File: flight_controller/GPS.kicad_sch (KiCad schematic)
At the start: 25 parts, among them CN2 A1251WV-S-6P, CN3 A1251WV-S-4P, CN5 A1251WV-S-3P, J16 A1257WV-S-6P-LCP, J17 HCZZ0494-2, Q2 AO3400A

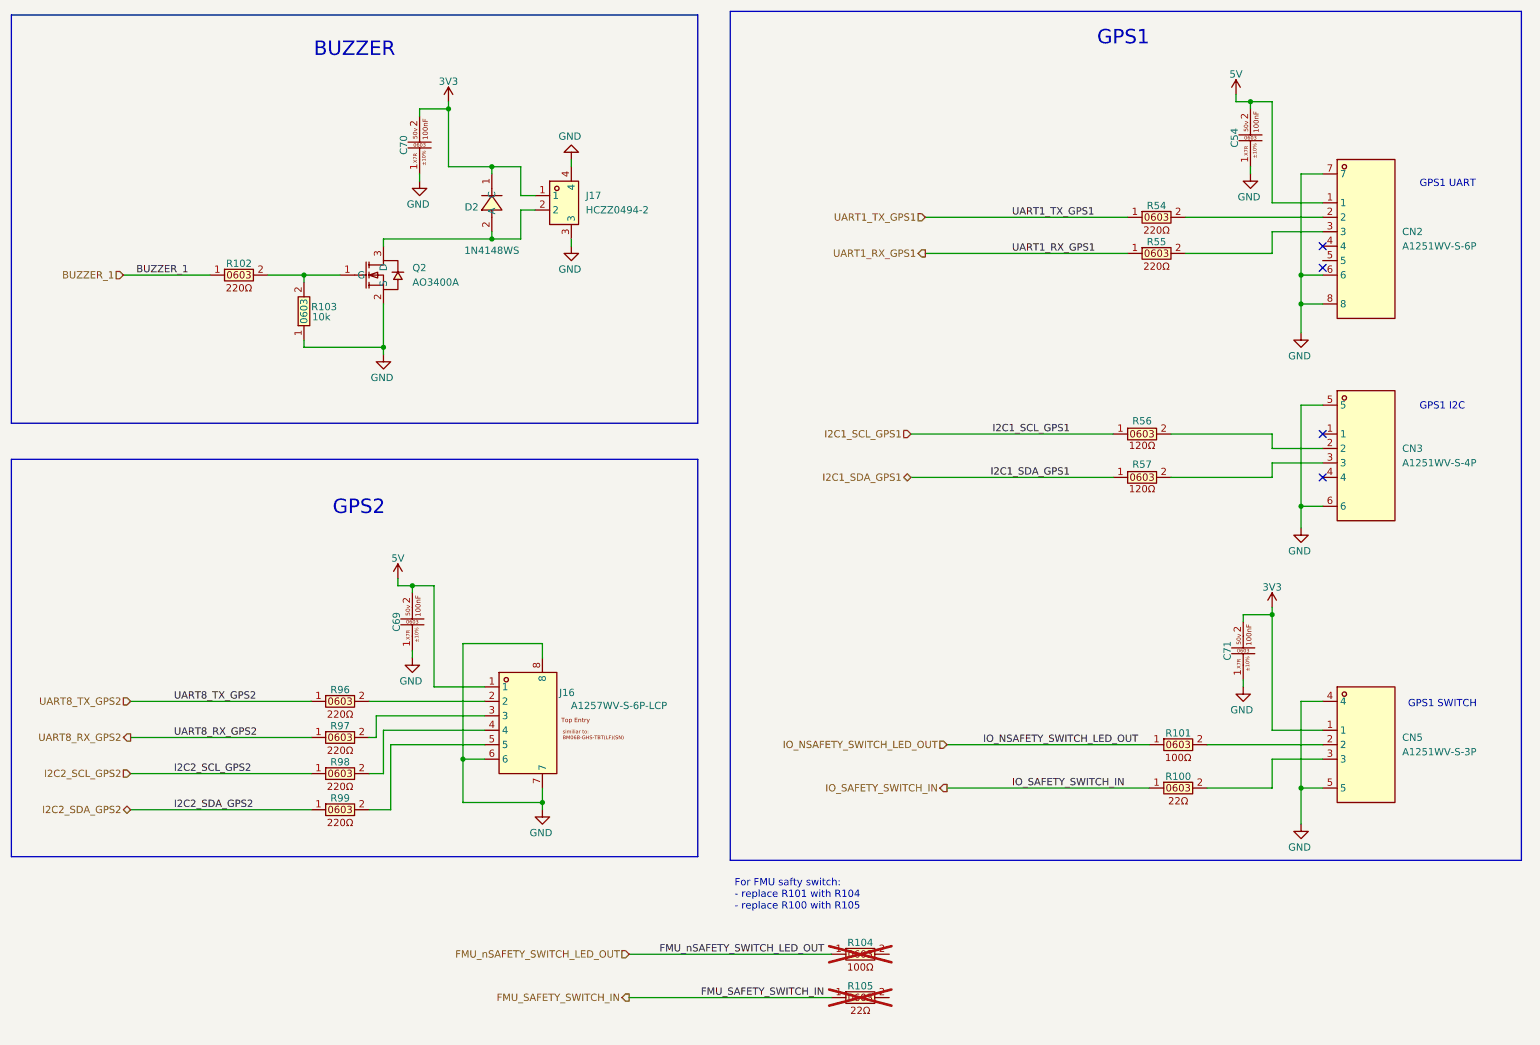
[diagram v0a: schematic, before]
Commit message: Schematic complete, ready for layout. Added USB, TPs, power conn, updated clocks, ran Rules Checker and general review
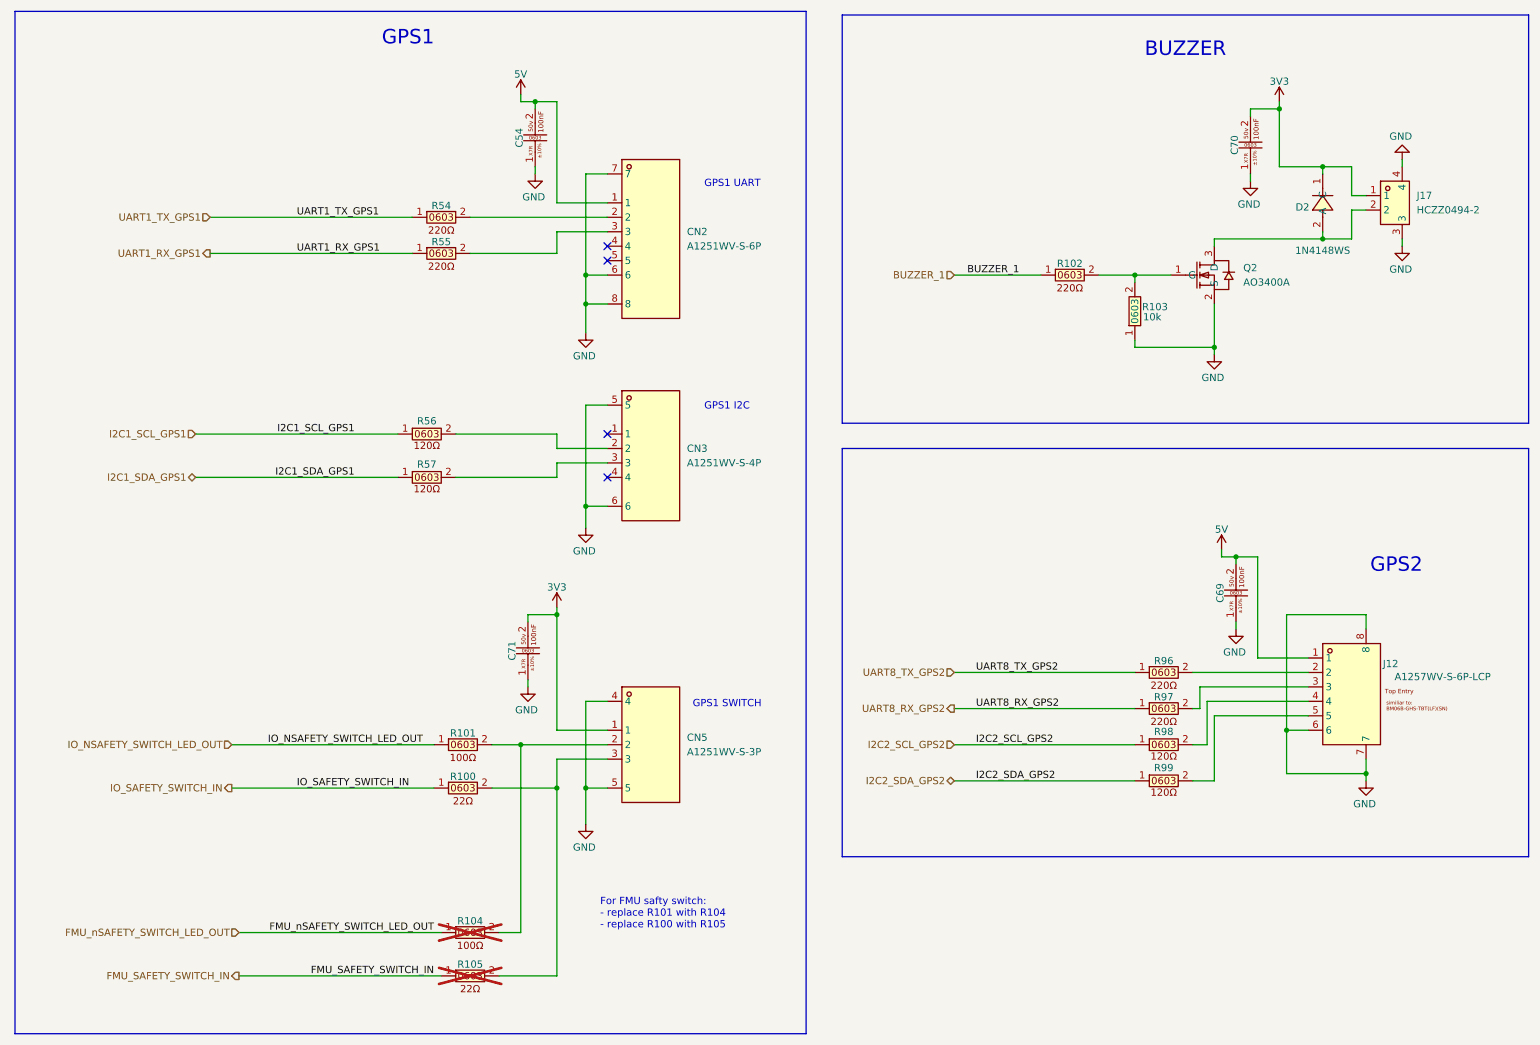
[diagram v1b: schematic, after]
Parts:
- removed J16: A1257WV-S-6P-LCP, easyeda2kicad:CONN-SMD_A1257WV-S-6P, symbol lampelKicadLIB:A1257WV-S-6P-LCP
- removed R98, R99: 0603WAF2200T5E (220ohm , 0603), easyeda2kicad:R0603, symbol lampelKicadLIB:0603WAF2200T5E (220ohm , 0603)
- added J12: A1257WV-S-6P-LCP, easyeda2kicad:CONN-SMD_A1257WV-S-6P, symbol lampelKicadLIB:A1257WV-S-6P-LCP
- added R98, R99: 603WAF1200T5E, easyeda2kicad:R0603, symbol lampelKicadLIB:0603WAF1200T5E (120ohm,0603)
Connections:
- net 5V: now also J12.1
- net GND: now also J12.6, J12.7, J12.8
- net I2C2_SCL_GPS2: now also R98.1
- net I2C2_SDA_GPS2: now also R99.1
- net at R96.2: now also J12.2
- net at R97.2: now also J12.3
- net at CN5.2, R101.2: now also R104.2
- net at CN5.3, R100.2: now also R105.2
- new net: J12.4, R98.2
- new net: J12.5, R99.2
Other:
- moved on the sheet: C54, C70, C71, CN2, CN3, CN5, D2, J17, Q2, R100, R101, R102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

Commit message: Started the placement process
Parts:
- renumbered C71 to C73, C54 to C74, C69 to C75, C70 to C76, CN2 to CN1, CN3 to CN2, CN5 to CN3, D2 to D5, J12 to J15, J17 to J16, Q2 to Q1, R56 to R86, R57 to R87, R54 to R88, R55 to R89, R101 to R90, R100 to R91, R104 to R92, R105 to R93, R102 to R94, R103 to R95

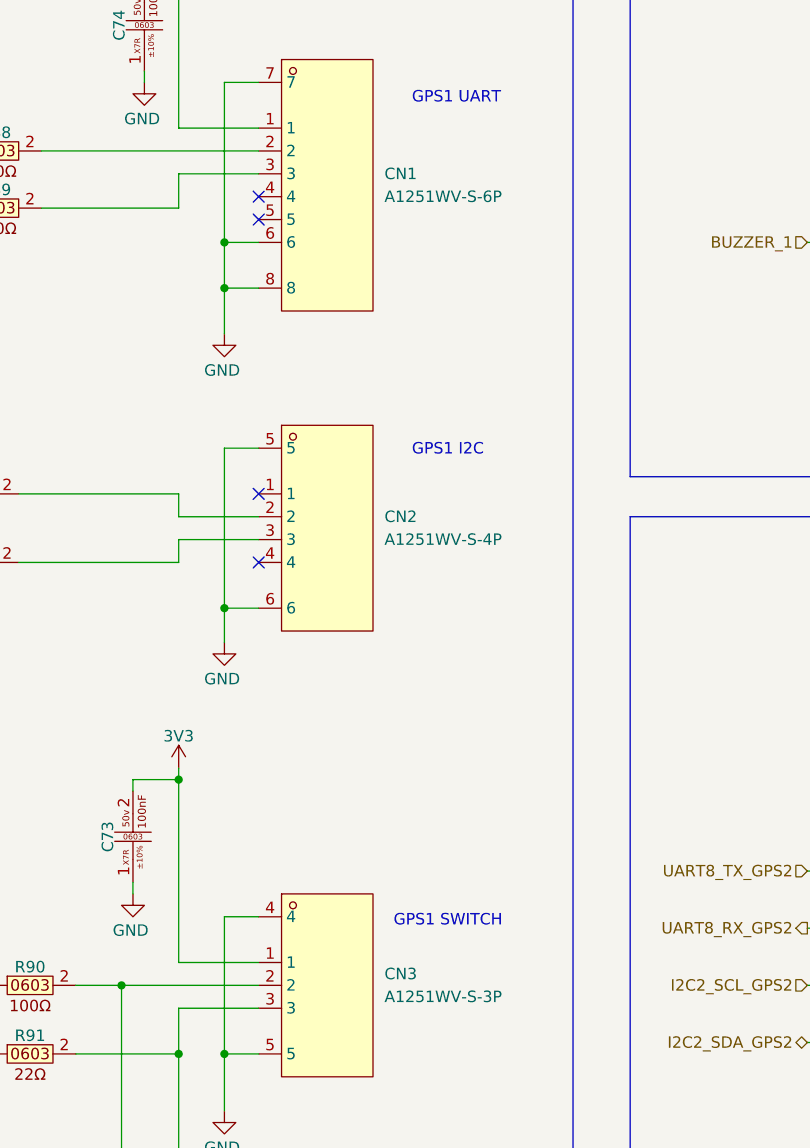
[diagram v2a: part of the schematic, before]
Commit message: renamed some connectors to j instead of cn
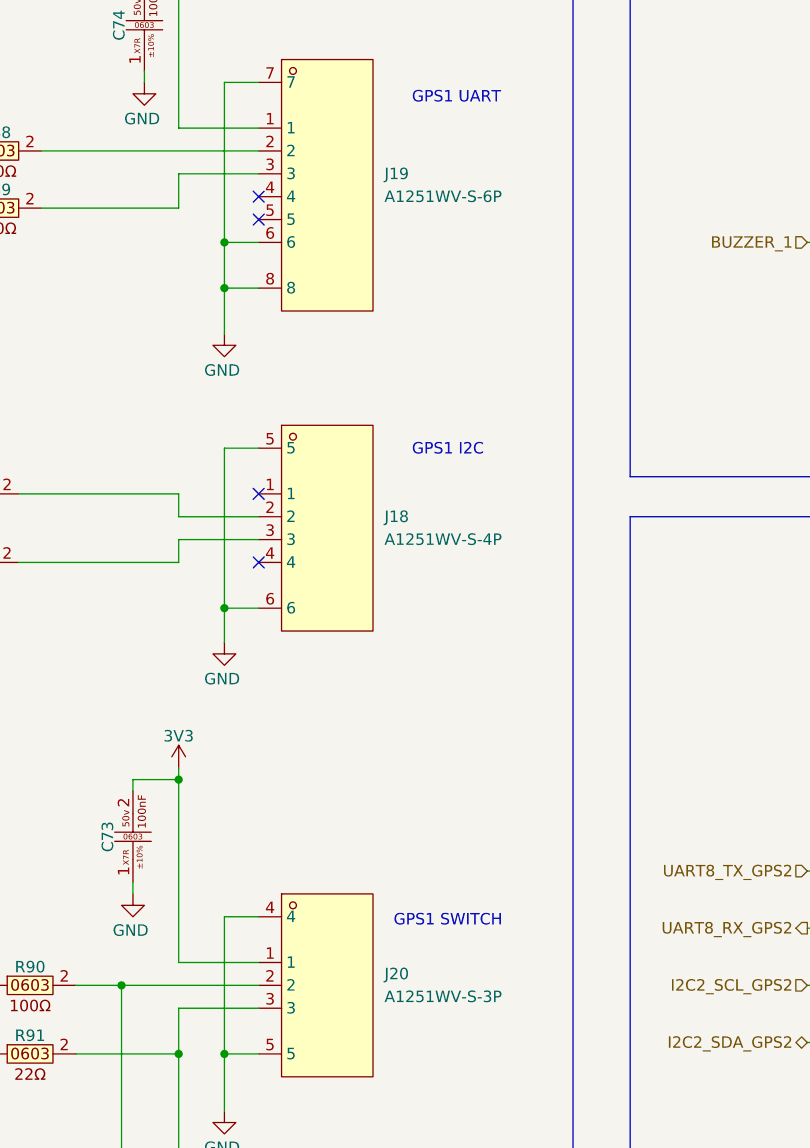
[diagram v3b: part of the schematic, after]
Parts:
- renumbered CN2 to J18, CN1 to J19, CN3 to J20
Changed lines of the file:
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@@
 		(dnp no)
 		(fields_autoplaced yes)
-		(property "Reference" "CN3"
+		(property "Reference" "J20"
 			(at 134.62 142.2399 0)
 			(effects
@@
 			(project "FP_BOARD"
 				(path "/17737359-1a8e-4237-8899-d9604030bc1d/31f9a705-a1ce-4496-8891-d4c27269046d"
-					(reference "CN3")
+					(reference "J20")
 					(unit 1)
 				)
@@
 		(dnp no)
 		(fields_autoplaced yes)
-		(property "Reference" "CN1"
+		(property "Reference" "J19"
 			(at 134.62 53.3399 0)
 			(effects
@@
 			(project "FP_BOARD"
 				(path "/17737359-1a8e-4237-8899-d9604030bc1d/31f9a705-a1ce-4496-8891-d4c27269046d"
-					(reference "CN1")
+					(reference "J19")
 					(unit 1)
 				)
@@
 		(dnp no)
 		(fields_autoplaced yes)
-		(property "Reference" "CN2"
+		(property "Reference" "J18"
 			(at 134.62 91.4399 0)
 			(effects
@@
 			(project "FP_BOARD"
 				(path "/17737359-1a8e-4237-8899-d9604030bc1d/31f9a705-a1ce-4496-8891-d4c27269046d"
-					(reference "CN2")
-					(unit 1)
-				)
+					(reference "J18")
+					(unit 1)
+				)
